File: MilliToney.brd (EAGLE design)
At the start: 50 x 50 mm, 72 parts, among them J1 BANANA_CONN, J2 BANANA_CONN, J3 BANANA_CONN, J4 BANANA_CONN, J5 BANANA_CONN, J6 BANANA_CONN, J7 BANANA_CONN, J8 BANANA_CONN, Q1 BC807-16LT1SMD, U1 OPA335AIDBVT, U2 TLV431BIDBZR

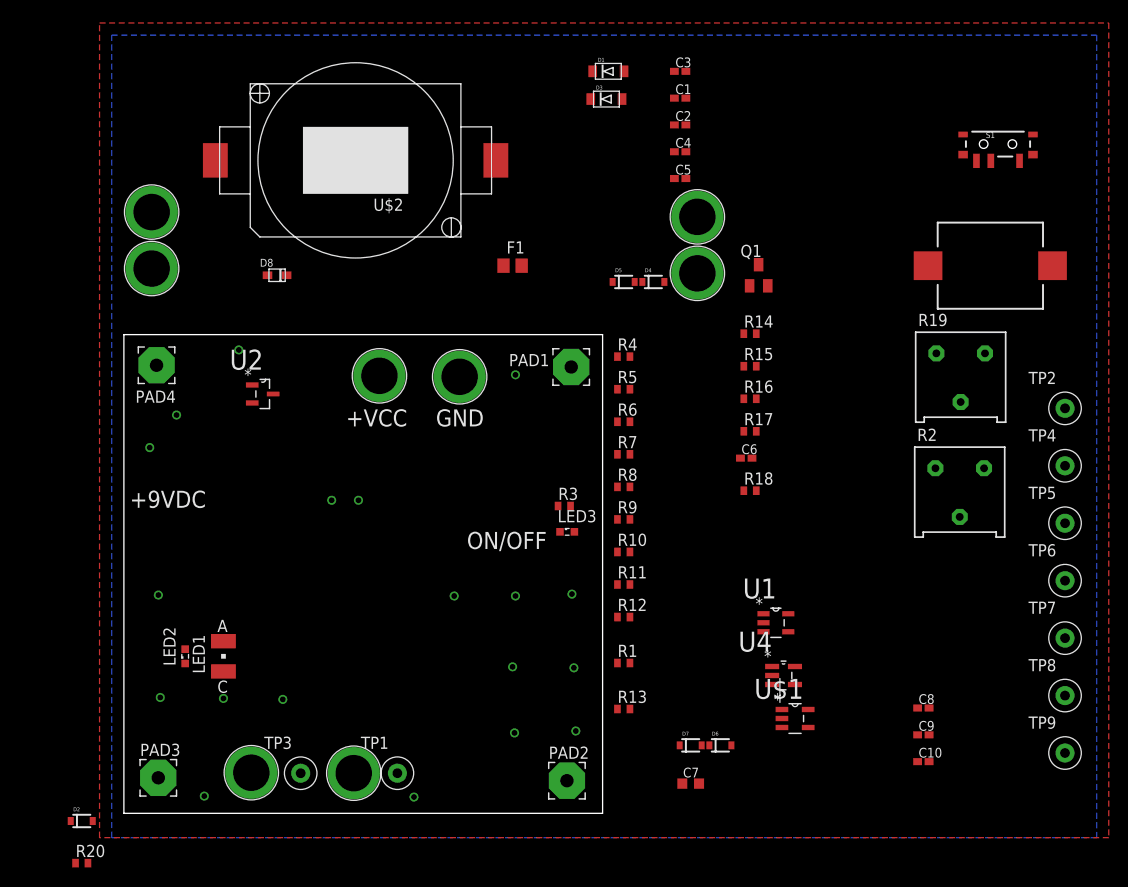
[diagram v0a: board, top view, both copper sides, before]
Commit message: Committing latest updates
Committing latest updates. dual footprints buzzer and battery, updated
other parts. added 5x5 footprint for board
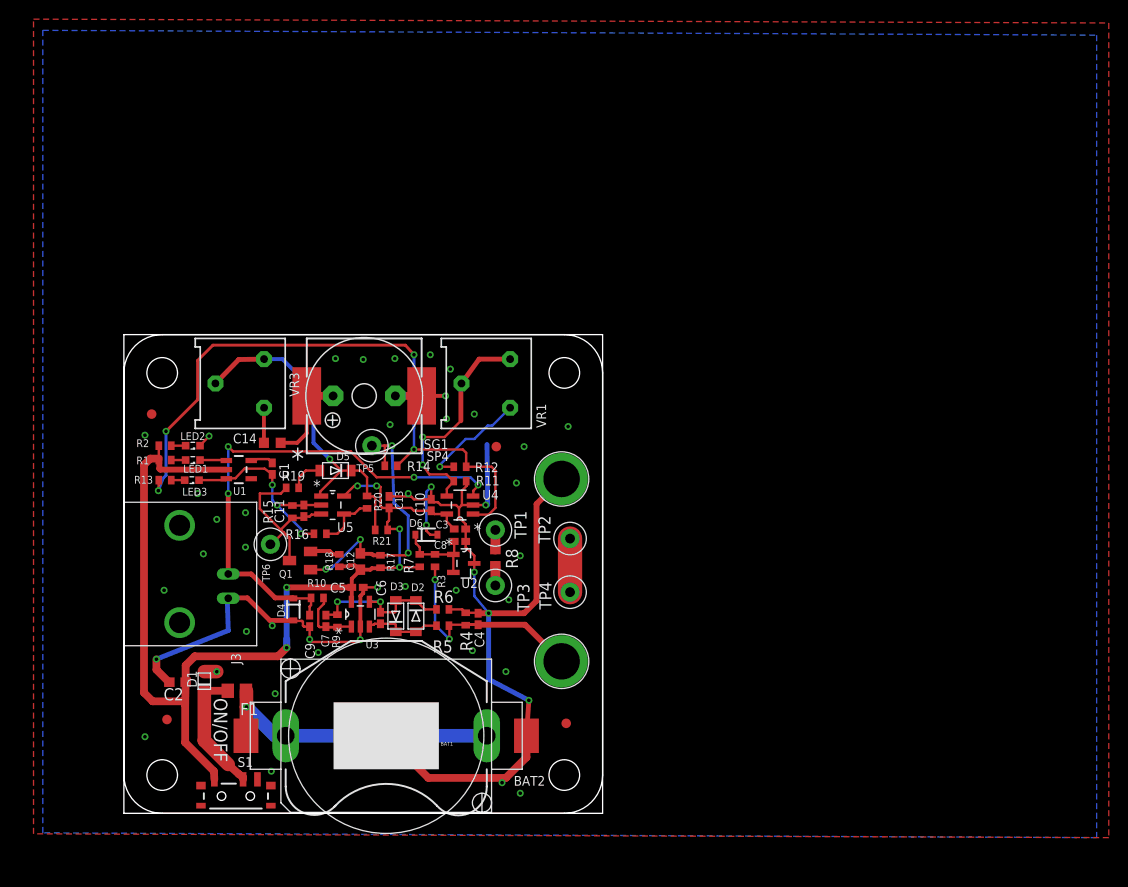
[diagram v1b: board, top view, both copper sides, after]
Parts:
- removed D7: 2.7V, SparkFun-DiscreteSemi:SOD-323
- removed D8: 0.5A SOD323F, adafruit:SOD-323F
- removed J4, J5, J6, J7, J8: BANANA_CONN, SparkFun-Connectors:BANANA_CONN
- removed PAD1, PAD2, PAD3, PAD4: MOUNT_HOLE, wirepad:3,81/1,4
- removed TP7, TP8, TP9: TP_1MM_TH", TP_1MM_TH:TP_1MM_TH
- added BAT1: CR2032, SparkFun-Electromechanical:BATTERY_20MM_PTH_COMPACT
- added BAT2: CR2032, kzh20_lithium_batterie_holder:KZH20SMD
- added C11: 10nF, rcl:C0402K
- added C12: 10uF, rcl:C0603
- added C13: 100nF, rcl:C0402K
- added C14: 10uF, rcl:C0603K
- added PCB1: PCB_DP_SQUARE-5X5, dp_devices:DP5050_V1
- added R21: 1k, rcl:R0402
- added SP4: KSS1201, buzzer:KSS1201
- added U$3, U$4: FIDUCIAL, adafruit:FIDUCIAL_1MM
- added U3: OPA335AIDBVT, Texas Instruments_By_element14_Batch_1:SOT95P280X145-5N
- added U5: Comparator, MCP6541_SOT23-5:SOT95P290X145-5N
- added VR1: (no value), bourns:3386F
- added VR3: 1k, bourns:3386F
- C1: value 100n -> DNF
- C10: value 100n -> 100nF
- C2: value 10n -> 10uF; device rcl:C0402K -> rcl:C0603
- C4: value 100p -> 470pF
- C5: value (none) -> 100n
- C6: value (none) -> 10n
- C7: value (none) -> 100p; device rcl:C0603K -> rcl:C0402K
- C9: value 100n -> 10n
- D1: value 1N4148W_SOD123 -> 0.5A SOD323F; device adafruit:SOD-123FL -> adafruit:SOD-323F
- D2, D5: value 2.7V -> 1N4148W_SOD123; device SparkFun-DiscreteSemi:SOD-323 -> adafruit:SOD-123FL
- J3: value BANANA_CONN -> BNCPTH; device SparkFun-Connectors:BANANA_CONN -> SparkFun-Connectors:BNC
- LED1: value GREEN_LED -> (none); device P-LCC-2_Shorter:P-LCC-2 -> led:SML0603
- R12: value NOFIT -> (none)
- R13: value (none) -> 2k
- R15, R4: value (none) -> 1M
- R16: value (none) -> 47k
- R17: value (none) -> 100k
- R18: value (none) -> 1k
- R19: value (none) -> 330R; device bourns:3386F -> rcl:R0402
- R2: value (none) -> 2k; device bourns:3386F -> rcl:R0402
- R20: value 2k -> 47k
- R8: device rcl:R0402 -> rcl:R0603
- SG1: value BUZZERSMD3 -> BUZZERBUZZER-KMTG1203; device SparkFun-Electromechanical:BUZZER-CMT1102 -> KMTG1203:BUZZER-KMTG1203
- U$1: value MCP6001T-E/OT -> FIDUCIAL; device Microchip_By_element14_Batch_1:SOT95P270X145-5N -> adafruit:FIDUCIAL_1MM
- U$2: value 2032 -> FIDUCIAL; device kzh20_lithium_batterie_holder:KZH20SMD -> adafruit:FIDUCIAL_1MM
- U1: value OPA335AIDBVT -> NCP303LSN09; device Texas Instruments_By_element14_Batch_1:SOT95P280X145-5N -> SparkFun-DigitalIC:SOT23-5
- U4: value (none) -> MCP6001T-E/OT; device MCP6541_SOT23-5:SOT95P290X145-5N -> Microchip_By_element14_Batch_1:SOT95P270X145-5N
- moved S1 104.8 mm to (11.7, 1.80), turned to 180 degrees
- moved R2 83.1 mm to (4.30, 38.4), turned to 180 degrees
- moved TP6 83.1 mm to (15.3, 28.1)
- moved C2 78.4 mm to (5.60, 13.7), turned to 180 degrees
- moved D1 76.4 mm to (8.40, 13.8), turned to 270 degrees
- moved TP5 72.9 mm to (25.9, 38.4)
- moved R19 70.7 mm to (17.6, 34.0), turned to 180 degrees
- moved SG1 66.8 mm to (25.1, 43.6)
- moved C9 65.2 mm to (19.4, 20.1), turned to 270 degrees
- moved U$2 61.6 mm to (4.50, 9.80), turned to 0 degrees
- moved U1 58.3 mm to (12.0, 35.9), turned to 270 degrees
- moved D3 58.3 mm to (28.4, 20.6), turned to 90 degrees
- moved C10 58.0 mm to (32.1, 32.2), turned to 270 degrees
- moved C1 57.6 mm to (15.5, 36.0), turned to 270 degrees
- moved Q1 56.4 mm to (18.4, 26.4), turned to 90 degrees
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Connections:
- removed net +2.5V_REF: J3.P$1, TP1.P$1
- removed net HI_OUT: J8.P$1, R9.1, TP4.P$1
- removed net HI_SENSE: C5.1, J1.P$1, R7.1, TP5.P$1
- removed net N$10: C4.2, D7.A, R5.1, R6.2, U1.1
- removed net N$12: R15.1, R16.1, R18.2, R19.2, TP8.P$1, U4.1
- removed net N$13: D5.A, R13.1, R20.1, R4.2, U$1.1
- new net N$24: C11.2, Q1.C, R15.1, R19.2, TP6.P$1, U5.3
- new net N$27: R8.2, TP1.P$1
- new net N$30: LED2.A, R2.1
- new net VIN: C4.1, J2.P$1, R3.1, R4.2, R5.1
- new net VOUTA: C7.2, R10.1, R9.2, U3.1
- new net VOUTB: C9.1, D4.C, J3.S, R10.2, U4.3
- new net VOUT_COMP: D5.C, R20.1, R21.2, U5.1, VR3.1, VR3.2
- new net VOUT_DRIVE: R12.2, R13.1, R14.1, U4.1
- new net VREF: C8.1, D6.C, R3.2, R7.1, U2.1, U2.2
- net GND: now also BAT1.2, BAT2.-, C11.1, C13.1, C3.1, C4.2, C5.1, C8.2, C9.2, D1.A, D4.A, D6.A, J1.P$1, J3.GND, LED2.C, R15.2, R16.2, R4.1, R6.1, SP4.-, U1.3, U3.2, U5.2; no longer C5.2, C6.1, C8.1, C9.1, D2.A, D8.A, J2.P$1, J5.P$1, J6.P$1, J7.P$1, LED1.C, PAD1.1, PAD2.1, PAD3.1, PAD4.1, R12.2, R17.2, R8.1, TP3.P$1, TP6.P$1, TP7.P$1, U$1.2, U$2.-, U1.2
- net N$1: now also BAT1.1, BAT2.+, F1.1; no longer S1.2, U$2.+
- net N$11: now also R12.1, VR1.3; no longer R2.2, R4.1
- net N$14: now also U4.4, VR1.1, VR1.2; no longer D4.A, R2.1, U$1.4
- net N$16: now also LED1.C, U1.1; no longer D4.C, D5.C
- net N$17: now also C12.2, R14.2, R17.2, TP5.P$1; no longer R13.2, R3.2
- net N$18: now also R18.1; no longer R14.1
- net N$19: now also D1.C, F1.2, S1.2; no longer C6.2, Q1.C, R15.2
- net N$20: now also C1.1, U1.5; no longer D6.C, D7.C
- net N$21: now also R16.1, R20.2, U5.4; no longer R16.2, R17.1
- net N$22: now also C14.1, VR3.3; no longer C7.1, R19.3, TP9.P$1
- net N$23: now also R13.2; no longer R20.2
- net N$3: now also C14.2, SP4.+; no longer C7.2
- net N$5: now also R8.1, TP3.P$1; no longer F1.1, S1.3
- net N$6: now also C6.2, D2.A, D3.C, R5.2, U3.3; no longer C3.2, D1.C, D3.A, R12.1, R7.2, U1.3
- net N$7: now also TP2.P$1, TP4.P$1; no longer C1.1, R10.1, R9.2, U2.1, U2.2
- net N$8: now also D5.A, R19.1; no longer C2.1, D2.C, J4.P$1, R5.2, TP2.P$1, U$1.3
- net N$9: now also C6.1, C7.1, D2.C, D3.A, R6.2, R9.1, U3.4; no longer C3.1, C4.1, D1.A, D3.C, D6.A, R6.1, R8.2, U1.4
- net VCC: now also C12.1, C13.2, C2.1, C3.2, C5.2, R17.1, R18.2, R2.2, R21.1, R7.2, S1.3, U1.2, U3.5, U5.5; no longer C8.2, C9.2, D8.C, F1.2, R10.2, R14.2, R18.1, R3.1, U$1.5, U1.5
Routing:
- net GND: track 0.00 -> 168.3 mm, vias 19 -> 49
- net VCC: track 0.00 -> 113.2 mm, vias 0 -> 6
- net VOUT_DRIVE: track 0.00 -> 69.2 mm, vias 0 -> 4
- net VOUTB: track 0.00 -> 54.0 mm, vias 0 -> 4
- net VOUT_COMP: track 0.00 -> 35.1 mm, vias 0 -> 1
- net N$1: track 0.00 -> 31.2 mm, vias 0 -> 1
- net N$17: track 0.00 -> 29.3 mm, vias 0 -> 4
- net VIN: track 0.00 -> 24.3 mm, vias 0 -> 2
- net N$14: track 0.00 -> 23.8 mm, vias 0 -> 2
- net N$24: track 0.00 -> 18.1 mm
- net N$9: track 0.00 -> 16.8 mm, vias 0 -> 2
- net N$19: track 0.00 -> 13.4 mm
- net N$11: track 0.00 -> 11.5 mm, vias 0 -> 1
- net N$3: track 0.00 -> 9.79 mm
- net VREF: track 0.00 -> 9.03 mm
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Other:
- board text removed: "+9VDC"
- board text removed: "+VCC"
- board text removed: "-=BATTERY HOLDER THIS SIDE=-"
- board text removed: "GND"
- board text removed: "OPEN SOURCE HARDWARE"

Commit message: Minor updates
Minor Updates
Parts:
- moved TP4 1.10 mm to (46.6, 22.0)
- moved TP2 0.90 mm to (46.6, 27.8)
- moved J2 0.43 mm to (45.7, 15.4)
- moved LOGO1 0.40 mm to (26.6, 16.1)
- moved J1 0.38 mm to (45.7, 34.5)
- moved C8 0.30 mm to (35.4, 28.4)
- moved U$3 0.22 mm to (2.80, 41.5)
- moved LED2 0.20 mm to (7.20, 38.6)
- moved R2 0.20 mm to (4.30, 38.6)
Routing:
- net GND: track 168.3 -> 166.6 mm, vias 49 -> 58
- net N$1: track 31.2 -> 32.9 mm
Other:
- outline, holes or cut-outs redrawn
- board text added: "MilliToney"
- board text removed: "MicroToney"

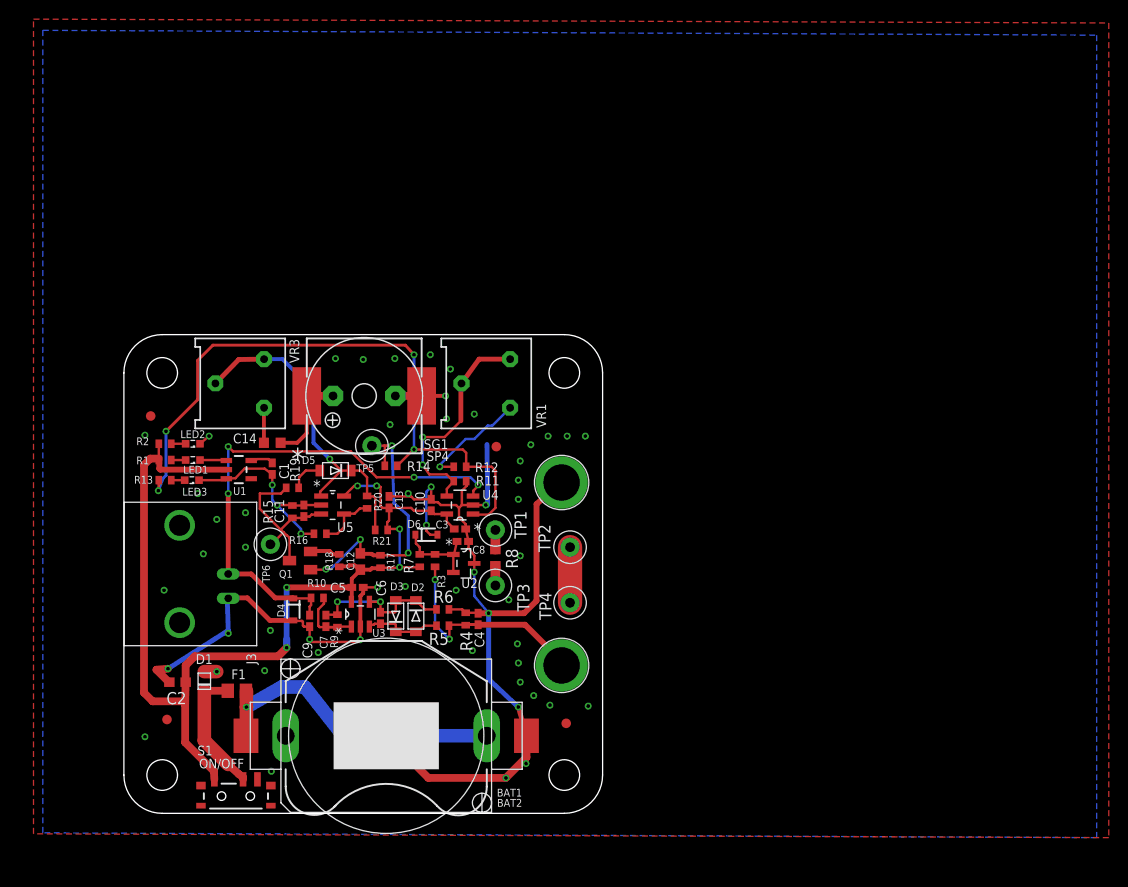
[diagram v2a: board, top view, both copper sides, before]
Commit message: CAD A Release Version
CAD A Release Version
Moved battery inboard requiring moving of various components
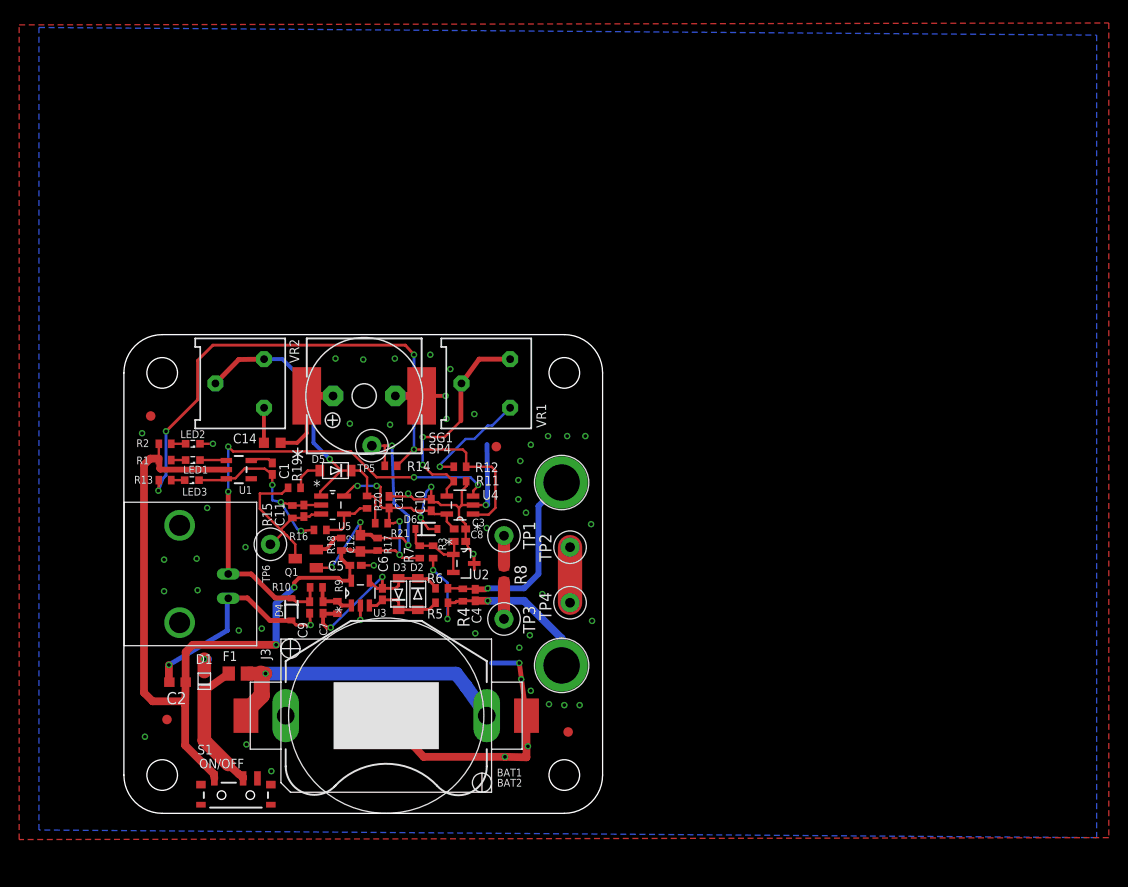
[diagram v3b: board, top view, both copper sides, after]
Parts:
- removed U$1: FIDUCIAL, adafruit:FIDUCIAL_1MM
- added FID1: FIDUCIAL, adafruit:FIDUCIAL_1MM
- moved TP3 3.61 mm to (39.7, 20.3)
- moved R4 2.52 mm to (35.4, 22.8)
- moved C4 2.52 mm to (36.7, 22.8)
- moved C6 2.51 mm to (27.0, 22.9)
- moved R5 2.40 mm to (33.2, 22.0)
- moved D3 2.32 mm to (28.7, 22.9)
- moved C5 2.31 mm to (24.2, 25.9)
- moved D2 2.31 mm to (30.7, 22.9)
- moved R6 2.20 mm to (33.2, 23.5)
- moved U3 2.20 mm to (24.7, 23.0)
- moved BAT1 2.10 mm to (27.4, 10.2)
- moved BAT2 2.10 mm to (27.4, 10.2)
- moved R8 1.92 mm to (39.7, 25.0)
- moved C12 1.90 mm to (24.7, 28.2)
- moved R17 1.82 mm to (26.5, 28.1)
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- renumbered U$2 to FID2, U$3 to FID3, U$4 to FID4, VR3 to VR2
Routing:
- net GND: track 166.6 -> 142.9 mm, vias 58 -> 60
- net N$9: track 16.8 -> 21.0 mm
- net VOUTA: track 7.93 -> 4.69 mm
- net N$5: track 2.05 -> 3.85 mm
- net VCC: track 113.4 -> 112.2 mm
- net N$27: track 2.05 -> 3.15 mm
- net VOUT_COMP: track 35.1 -> 34.4 mm
- net N$17: track 29.3 -> 29.8 mm
- net N$19: track 13.4 -> 14.0 mm
- net N$18: track 3.15 -> 3.68 mm
- net N$1: track 32.9 -> 32.4 mm
- net VIN: track 24.7 -> 25.2 mm, vias 2 -> 3

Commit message: minor movement on the schematic
minor movement on the schematic
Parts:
- C10, C13: value 100nF -> 100n
- C11: value 10nF -> 10n
- C12, C14, C2: value 10uF -> 10u
- C4: value 470pF -> 470p
- J3: value BNCPTH -> TE 5227161-1
- R8: value (none) -> 0.1R
- SP4: value KSS1201 -> SPKR_PTH_6.5MM_PITCH

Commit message: Updated part values and part number
Updated part values and part number
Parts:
- D4: value 2.7V -> 3.3V
- D6: value 2.7V -> DNF
- J1: value BANANA_CONN -> BANANA_CONN_BLACK
- J2: value BANANA_CONN -> BANANA_CONN_RED
- LED1: value (none) -> Red LED
- LED2: value (none) -> Green LED
- LED3: value (none) -> Yellow LED
- R1, R13, R2: value 2k -> 2k 5%
- R10, R11: value (none) -> 100R 5%
- R12: value (none) -> 0R0
- R14: value (none) -> 2k 5%
- R15, R4: value 1M -> 1M 5%
- R16, R20: value 47k -> 47k 5%
- R17: value 100k -> 100k 5%
- R18, R21: value 1k -> 1k 5%
- R19: value 330R -> 330R 5%
- R3: value (none) -> 619R 0.1%
- R5: value (none) -> 1k 1%
- R6: value (none) -> 1k 0.1%
- R7: value (none) -> 150R 5%
- R8: value 0.1R -> 0.1R 1%
- R9: value (none) -> 499k 1%
- VR1: value (none) -> 100k 10%
- VR2: value 1k -> 1k 10%

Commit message: updated layout and parts
updated layout and parts
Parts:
- BAT1: value CR2032 -> DNF CR2032
- R18, R21: value 1k 5% -> 1k 1%
- U5: value Comparator -> MCP6541T-I/OT
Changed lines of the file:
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@@
 <attribute name="MPN" value="BC807-16LT1G" x="19" y="26.6" size="1.778" layer="27" rot="R90" display="off"/>
 </element>
-<element name="R18" library="rcl" package="R0402" value="1k 5%" x="22.7" y="28.1" smashed="yes" rot="R270">
+<element name="R18" library="rcl" package="R0402" value="1k 1%" x="22.7" y="28.1" smashed="yes" rot="R270">
 <attribute name="NAME" x="21.235" y="29.035" size="0.8128" layer="25" rot="R270"/>
 <attribute name="VALUE" x="20.795" y="28.735" size="1.27" layer="27" rot="R270"/>
@@
 <attribute name="MPN" value="" x="18.8" y="31.6" size="1.778" layer="27" rot="R270" display="off"/>
 </element>
-<element name="R21" library="rcl" package="R0402" value="1k 5%" x="26.9" y="30.3" smashed="yes" rot="R180">
+<element name="R21" library="rcl" package="R0402" value="1k 1%" x="26.9" y="30.3" smashed="yes" rot="R180">
 <attribute name="NAME" x="29.835" y="29.665" size="0.8128" layer="25" rot="R180"/>
 <attribute name="VALUE" x="27.535" y="32.205" size="1.27" layer="27" rot="R180"/>
@@
 <attribute name="MPN" value="GRM188R61A106ME69D" x="15.5" y="38.7" size="1.778" layer="27" display="off"/>
 </element>
-<element name="U5" library="MCP6541_SOT23-5" package="SOT95P290X145-5N" value="Comparator" x="21.8" y="32.2" smashed="yes">
+<element name="U5" library="MCP6541_SOT23-5" package="SOT95P290X145-5N" value="MCP6541T-I/OT" x="21.8" y="32.2" smashed="yes">
 <attribute name="PACKAGE" value="SOT23-5" x="21.8" y="32.2" size="1.778" layer="27" display="off"/>
 <attribute name="OC_NEWARK" value="12T7776" x="21.8" y="32.2" size="1.778" layer="27" display="off"/>
@@
 <attribute name="VALUE" x="28.656" y="47.41" size="1.27" layer="27" ratio="10" rot="R180"/>
 </element>
-<element name="BAT1" library="SparkFun-Electromechanical" package="BATTERY_20MM_PTH_COMPACT" value="CR2032" x="27.4" y="10.2" smashed="yes" rot="R180">
+<element name="BAT1" library="SparkFun-Electromechanical" package="BATTERY_20MM_PTH_COMPACT" value="DNF   CR2032" x="27.4" y="10.2" smashed="yes" rot="R180">
 <attribute name="NAME" x="41.585" y="4.665" size="0.8128" layer="25" rot="R180"/>
 <attribute name="VALUE" x="34.385" y="10.835" size="0.4064" layer="27" rot="R180"/>
